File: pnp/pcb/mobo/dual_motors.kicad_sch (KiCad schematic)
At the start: 18 parts, among them J30 TMC_PIN_HEADER, M5 MOTOR1, M6 MOTOR2

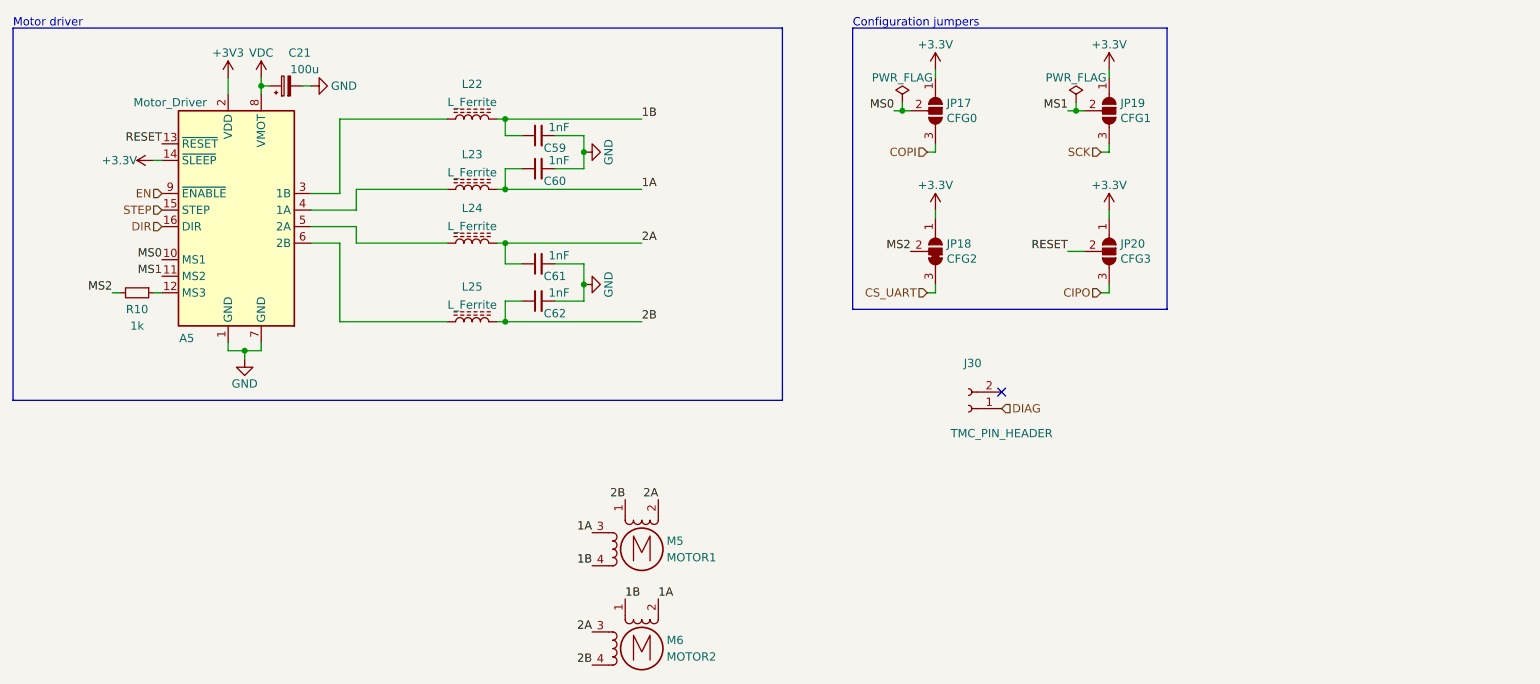
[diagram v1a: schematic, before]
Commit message: Redesign finished
Completed Board redesign and adding more EMC improvements.
Changed all the part numbers to have a Mouser orderable design (except the JST connectors)
All outputs generated
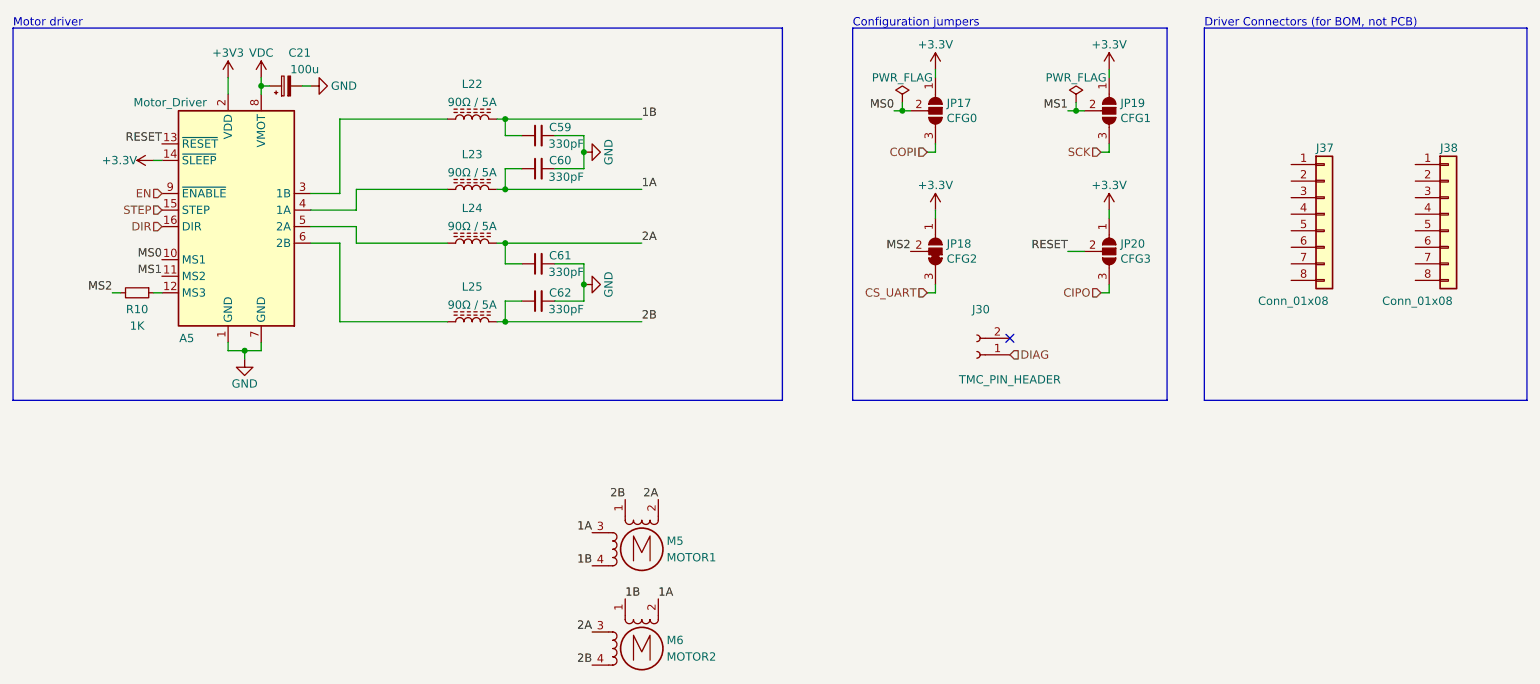
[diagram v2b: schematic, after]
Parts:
- added J37, J38: Conn_01x08, symbol Connector_Generic:Conn_01x08
- C21: Digikey 493-2203-1-ND -> (none); JLCPCB C99837 -> (none); LCSC C3339 -> (none); Mouser 647-UWT1V101MCL1S -> 710-865080545012; Voltage (none) -> 35V
- C59, C60, C61, C62: value 1nF -> 330pF; Mouser (none) -> 80-C0805C331K5RAC; Tolerance (none) -> 10%; Voltage (none) -> 50V
- J30: Mouser (none) -> 571-215297-2
- JP17, JP18, JP19, JP20: Mouser (none) -> -
- L22, L23, L24, L25: value L_Ferrite -> 90Ω / 5A; Mouser (none) -> 70-ILHB0805ER900V
- M5, M6: JLCPCB C37815 -> (none); LCSC C37815 -> (none); Mouser (none) -> Digikey
- R10: value 1k -> 1K; JLCPCB C17513 -> (none); LCSC C17513 -> (none); Mouser (none) -> 756-WCR0805-1K0FI
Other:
- note added: "Driver Connectors (for BOM, not PCB)"
- company: Opulo -> Opulo.io
- moved on the sheet: J30
